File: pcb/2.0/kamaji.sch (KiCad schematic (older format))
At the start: 44 parts, among them J1 RJ10, J2 RJ10, J3 RJ10, J4 RJ10, J5 RJ10, J6 Daughter board, J7 ICSP, J8 USB_B, J9 USB_A, Q1 IRL540N, Q2 IRL540N, Q3 IRL540N, SW1 SW_Push, SW2 SW_Push, SW3 SW_Push, U1 ATMEGA32U4-AU, Y1 16MHz

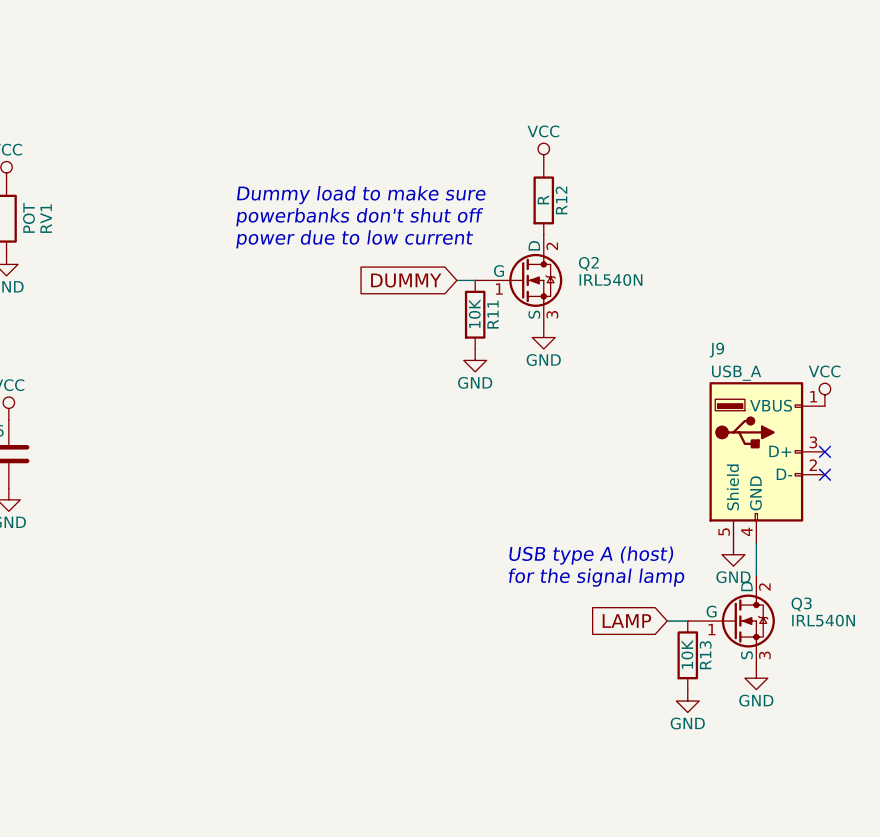
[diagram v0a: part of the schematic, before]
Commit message: use 4 parallel resistors for the dummy load
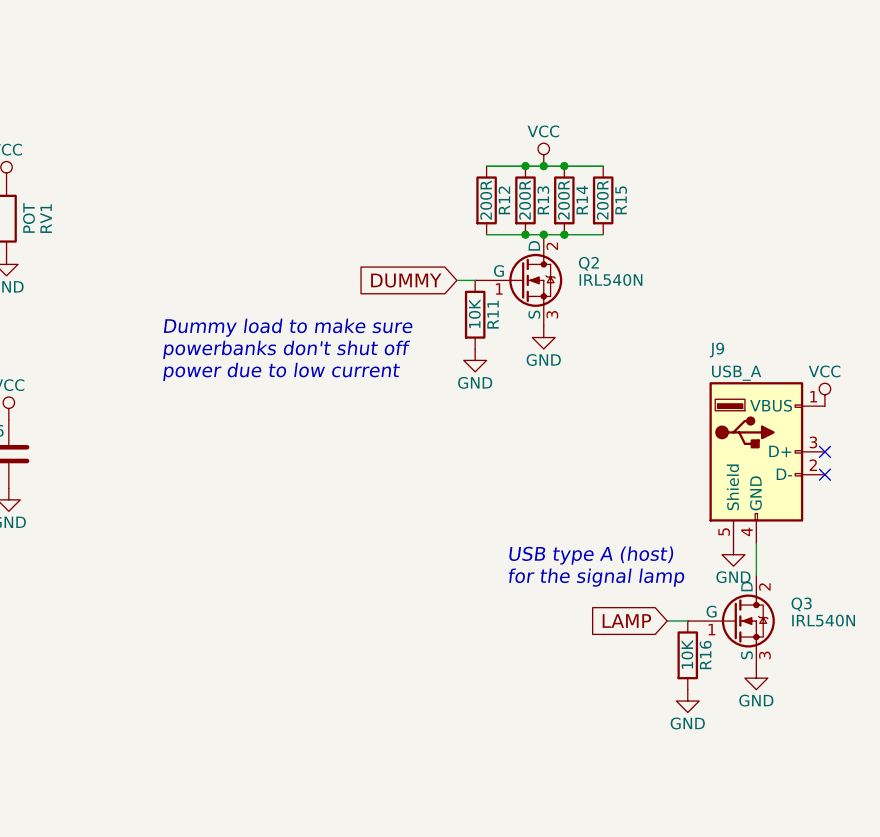
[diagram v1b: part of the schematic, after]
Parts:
- added R12, R13, R15: 200R, symbol R
- R14: renamed from R12; value R -> 200R
- renumbered R13 to R16
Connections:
- wire segments 82 -> 84
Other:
- moved on the sheet: R14

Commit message: start mapping symbols to footprints
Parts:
- F1: value 500mA -> 1A
- Q1, Q2, Q3: footprint TO_SOT_Packages_THT:TO-220_Vertical -> TO_SOT_Packages_THT:TO-220-3_Horizontal
- RV1: value POT -> 10K
- U1: footprint TQFP44 -> Housings_QFP:TQFP-44_10x10mm_Pitch0.8mm
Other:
- note added: "Control buttons use the internal pull-ups"

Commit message: use a graphic display instead of 2004
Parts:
- removed C6: 0.1uF, symbol C
- removed DS1: WC1602A, Displays:WC1602A, symbol WC1602A
- removed RV1: 10K, symbol POT
- added DS1: LCD12864B, kamaji:LCD12864B, symbol LCD12864B
- added R17, R18: 10K, symbol R
- R9: value 220R -> 10K
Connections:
- net labels added: LCD_CS, LCD_RST
- net labels removed: LCD_D4, LCD_D5, LCD_D6, LCD_D7, LCD_EN, LCD_RS
- wire segments 84 -> 80
- no-connect marks 3 -> 9
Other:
- note added: "Break for current\nmeasurement"
- note added: "Disconnect speaker\nwhen programmimg\nto avoid interference"
- note added: "ST7920-based LCD\ndisplay in serial mode"
- note removed: "Any HD44780 compatible LCD"
- moved on the sheet: F1, Q2, R11, R12, R13, R14, R15

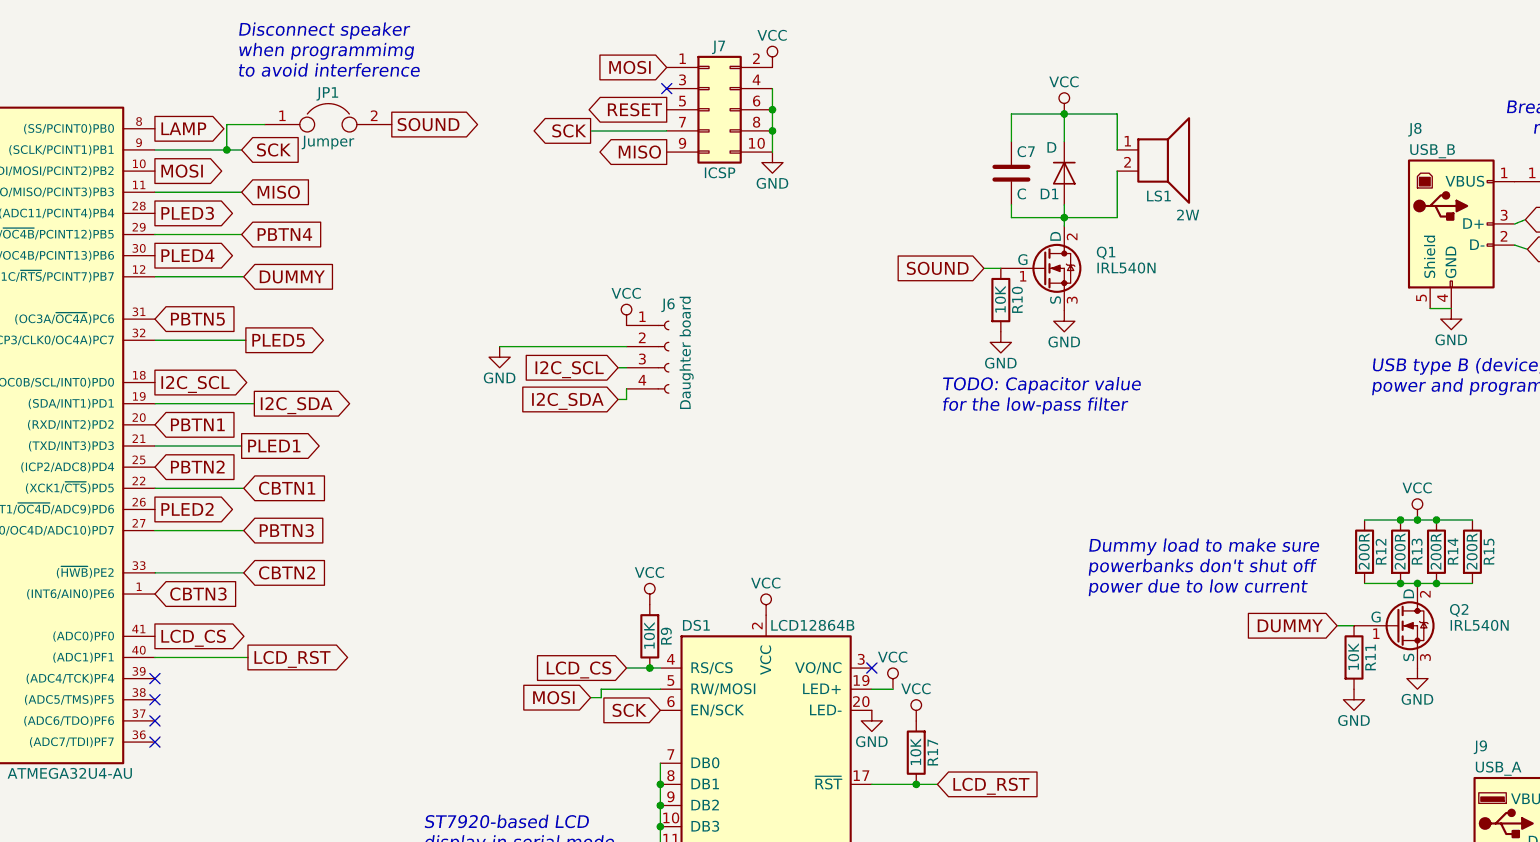
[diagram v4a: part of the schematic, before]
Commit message: pcb: delete the sound circuit
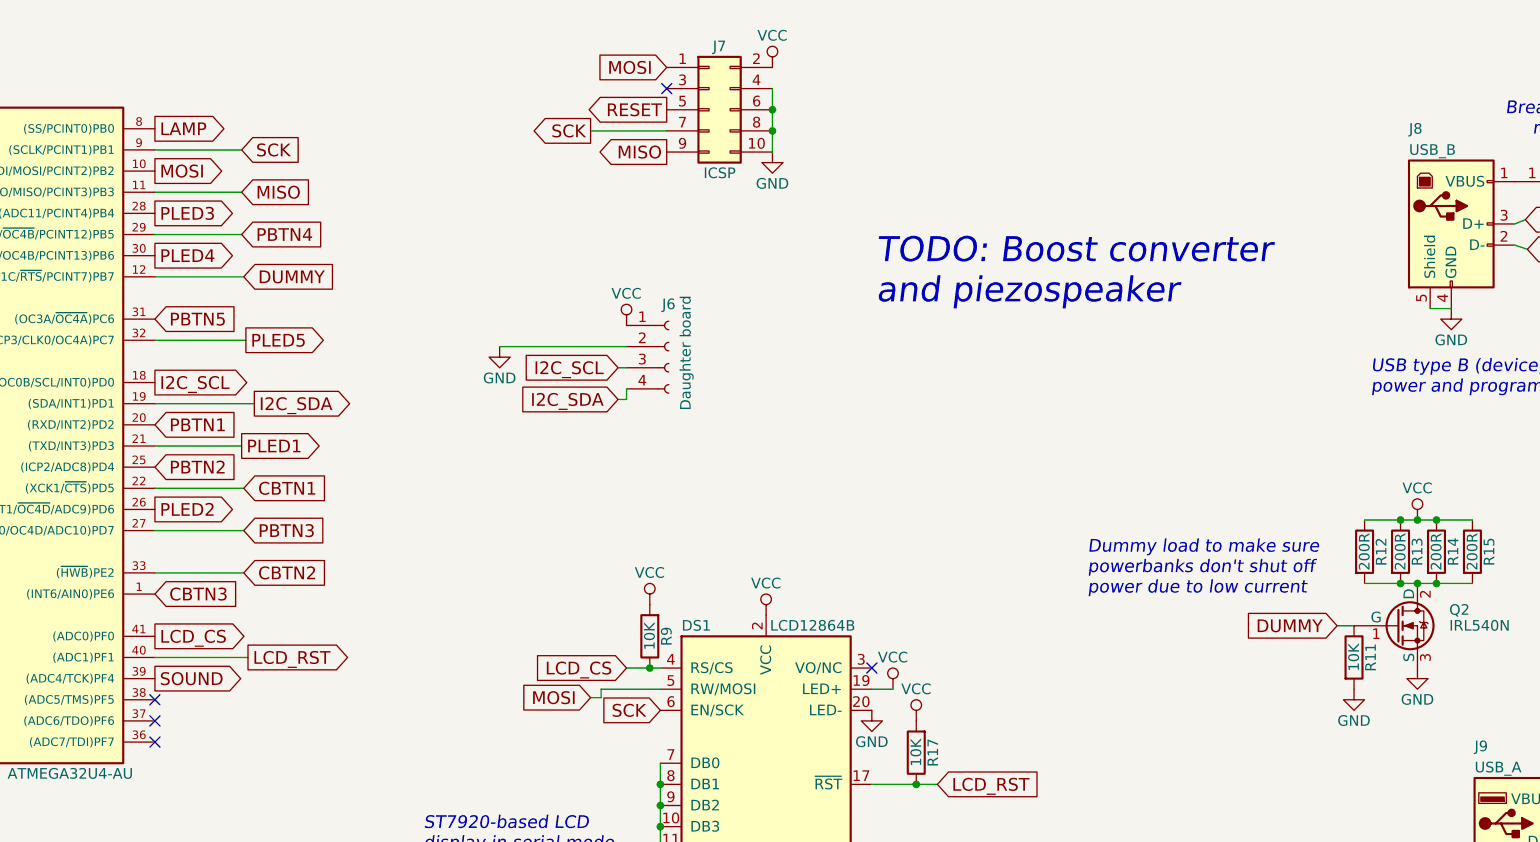
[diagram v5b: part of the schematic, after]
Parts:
- removed C7: C, symbol C
- removed D1: D, symbol D
- removed JP1: Jumper, symbol Jumper
- removed LS1: 2W, symbol Speaker
- removed Q1: IRL540N, TO_SOT_Packages_THT:TO-220-3_Horizontal, symbol IRLIZ44N
- removed R10: 10K, symbol R
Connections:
- net SOUND: now also U1.39 ((ADC4/TCK)PF4)
- no-connect marks 9 -> 8
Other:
- note added: "TODO: Boost converter\nand piezospeaker"
- note removed: "Disconnect speaker\nwhen programmimg\nto avoid interference"
- note removed: "TODO: Capacitor value\nfor the low-pass filter"
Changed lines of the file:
@@
 LIBS:kamaji
 LIBS:switches
+LIBS:kamaji-cache
 EELAYER 25 0
 EELAYER END
@@
 $EndComp
 $Comp
-L Speaker LS1
-U 1 1 59EB0736
-P 8480 1580
-F 0 "LS1" H 8540 1360 50  0000 R CNN
-F 1 "2W" H 8670 1270 50  0000 R CNN
-F 2 "" H 8480 1380 50  0001 C CNN
-F 3 "" H 8470 1530 50  0001 C CNN
-	1    8480 1580
-	1    0    0    -1
-$EndComp
-$Comp
-L D D1
-U 1 1 59EB079D
-P 8030 1690
-F 0 "D1" V 8130 1620 50  0000 C CNN
-F 1 "D" V 7910 1630 50  0000 C CNN
-F 2 "" H 8030 1690 50  0001 C CNN
-F 3 "" H 8030 1690 50  0001 C CNN
-	1    8030 1690
-	0    1    1    0
-$EndComp
-$Comp
-L VCC #PWR09
-U 1 1 59EB08CE
-P 8030 1410
-F 0 "#PWR09" H 8030 1260 50  0001 C CNN
-F 1 "VCC" H 8030 1560 50  0000 C CNN
-F 2 "" H 8030 1410 50  0001 C CNN
-F 3 "" H 8030 1410 50  0001 C CNN
-	1    8030 1410
-	1    0    0    -1
-$EndComp
-$Comp
-L C C7
-U 1 1 59EB0A92
-P 7780 1690
-F 0 "C7" H 7805 1790 50  0000 L CNN
-F 1 "C" H 7805 1590 50  0000 L CNN
-F 2 "" H 7818 1540 50  0001 C CNN
-F 3 "" H 7780 1690 50  0001 C CNN
-	1    7780 1690
-	1    0    0    -1
-$EndComp
-$Comp
-L IRLIZ44N Q1
-U 1 1 59EB0BD7
-P 7930 2140
-F 0 "Q1" H 8180 2215 50  0000 L CNN
-F 1 "IRL540N" H 8180 2140 50  0000 L CNN
-F 2 "TO_SOT_Packages_THT:TO-220-3_Horizontal" H 8180 2065 50  0001 L CIN
-F 3 "" H 7930 2140 50  0001 L CNN
-	1    7930 2140
-	1    0    0    -1
-$EndComp
-$Comp
-L GND #PWR010
-U 1 1 59EB0F4B
-P 8030 2340
-F 0 "#PWR010" H 8030 2090 50  0001 C CNN
-F 1 "GND" H 8030 2190 50  0000 C CNN
-F 2 "" H 8030 2340 50  0001 C CNN
-F 3 "" H 8030 2340 50  0001 C CNN
-	1    8030 2340
-	1    0    0    -1
-$EndComp
-$Comp
-L R R10
-U 1 1 59EB0FF4
-P 7730 2290
-F 0 "R10" V 7810 2290 50  0000 C CNN
-F 1 "10K" V 7730 2290 50  0000 C CNN
-F 2 "" V 7660 2290 50  0001 C CNN
-F 3 "" H 7730 2290 50  0001 C CNN
-	1    7730 2290
-	1    0    0    -1
-$EndComp
-$Comp
-L GND #PWR011
-U 1 1 59EB105E
-P 7730 2440
-F 0 "#PWR011" H 7730 2190 50  0001 C CNN
-F 1 "GND" H 7730 2290 50  0000 C CNN
-F 2 "" H 7730 2440 50  0001 C CNN
-F 3 "" H 7730 2440 50  0001 C CNN
-	1    7730 2440
-	1    0    0    -1
-$EndComp
-Text GLabel 7650 2140 0    60   Input ~ 0
-SOUND
-$Comp
 L Conn_02x05_Odd_Even J7
 U 1 1 59EB13A5
@@
 Text GLabel 6150 1190 0    60   Input ~ 0
 MOSI
-Text Notes 7450 2830 0    60   Italic 0
-TODO: Capacitor value\nfor the low-pass filter
 NoConn ~ 6150 1290
 $Comp
@@
 Text GLabel 4140 1580 2    60   Input ~ 0
 SCK
-$Comp
-L Jumper JP1
-U 1 1 59EB71E9
-P 4550 1460
-F 0 "JP1" H 4550 1610 50  0000 C CNN
-F 1 "Jumper" H 4550 1380 50  0000 C CNN
-F 2 "" H 4550 1460 50  0001 C CNN
-F 3 "" H 4550 1460 50  0001 C CNN
-	1    4550 1460
-	1    0    0    -1
-$EndComp
-Text GLabel 4850 1460 2    60   Output ~ 0
+Text GLabel 3730 4080 2    60   Output ~ 0
 SOUND
 $Comp
@@
 	9320 3830 9400 3830
 Wire Wire Line
-	7780 1410 8280 1410
-Wire Wire Line
-	8280 1410 8280 1580
-Wire Wire Line
-	7780 1540 7780 1410
-Wire Wire Line
-	8030 1840 8030 1940
-Wire Wire Line
-	8030 1540 8030 1410
-Connection ~ 8030 1410
-Wire Wire Line
-	7650 2140 7730 2140
-Wire Wire Line
 	6650 1290 6650 1590
 Connection ~ 6650 1390
@@
 	10210 1910 10160 1930
 Wire Wire Line
-	7780 1840 7780 1900
-Wire Wire Line
-	7780 1900 8280 1900
-Connection ~ 8030 1900
-Wire Wire Line
-	8280 1900 8280 1680
-Wire Wire Line
 	1600 7050 1750 7050
 Wire Wire Line
@@
 Wire Wire Line
 	3730 1580 4140 1580
-Wire Wire Line
-	4250 1460 4070 1460
-Wire Wire Line
-	4070 1460 4070 1580
-Connection ~ 4070 1580
 Wire Wire Line
 	9450 3630 9960 3630
@@
 Wire Wire Line
 	4170 3980 3730 3980
-NoConn ~ 3730 4080
 NoConn ~ 3730 4180
 NoConn ~ 3730 4280
@@
 	1    0    0    -1
 $EndComp
-Text Notes 4120 1250 0    60   Italic 0
-Disconnect speaker\nwhen programmimg\nto avoid interference
 Wire Wire Line
 	10940 1730 10760 1730
 Text Notes 10820 1520 2    60   Italic 0
 Break for current\nmeasurement
+Text Notes 7140 2320 0    118  Italic 0
+TODO: Boost converter\nand piezospeaker
 $EndSCHEMATC

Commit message: minor pcb changes
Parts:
- added C?: 0.1uF, symbol C
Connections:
- net GND: now also C?.2
- net VCC: now also C?.1
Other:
- moved on the sheet: C3, C4
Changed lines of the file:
@@
 L C C3
 U 1 1 59EB7B64
-P 1030 4610
-F 0 "C3" H 920 4710 50  0000 L CNN
-F 1 "0.1uF" H 790 4520 50  0000 L CNN
-F 2 "" H 1068 4460 50  0001 C CNN
-F 3 "" H 1030 4610 50  0001 C CNN
-	1    1030 4610
+P 910 5010
+F 0 "C3" H 800 5110 50  0000 L CNN
+F 1 "0.1uF" H 670 4920 50  0000 L CNN
+F 2 "" H 948 4860 50  0001 C CNN
+F 3 "" H 910 5010 50  0001 C CNN
+	1    910  5010
 	1    0    0    -1
 $EndComp
@@
 L GND #PWR034
 U 1 1 59EB7C3A
-P 1030 4760
-F 0 "#PWR034" H 1030 4510 50  0001 C CNN
-F 1 "GND" H 1030 4610 50  0000 C CNN
-F 2 "" H 1030 4760 50  0001 C CNN
-F 3 "" H 1030 4760 50  0001 C CNN
-	1    1030 4760
+P 910 5160
+F 0 "#PWR034" H 910 4910 50  0001 C CNN
+F 1 "GND" H 910 5010 50  0000 C CNN
+F 2 "" H 910 5160 50  0001 C CNN
+F 3 "" H 910 5160 50  0001 C CNN
+	1    910  5160
 	1    0    0    -1
 $EndComp
@@
 L VCC #PWR035
 U 1 1 59EB7CBD
-P 1030 4460
-F 0 "#PWR035" H 1030 4310 50  0001 C CNN
-F 1 "VCC" H 1030 4610 50  0000 C CNN
-F 2 "" H 1030 4460 50  0001 C CNN
-F 3 "" H 1030 4460 50  0001 C CNN
-	1    1030 4460
+P 910 4860
+F 0 "#PWR035" H 910 4710 50  0001 C CNN
+F 1 "VCC" H 910 5010 50  0000 C CNN
+F 2 "" H 910 4860 50  0001 C CNN
+F 3 "" H 910 4860 50  0001 C CNN
+	1    910  4860
 	1    0    0    -1
 $EndComp
@@
 L C C4
 U 1 1 59EB7D86
-P 1390 4610
-F 0 "C4" H 1280 4710 50  0000 L CNN
-F 1 "0.1uF" H 1150 4520 50  0000 L CNN
-F 2 "" H 1428 4460 50  0001 C CNN
-F 3 "" H 1390 4610 50  0001 C CNN
-	1    1390 4610
+P 1270 5010
+F 0 "C4" H 1160 5110 50  0000 L CNN
+F 1 "0.1uF" H 1030 4920 50  0000 L CNN
+F 2 "" H 1308 4860 50  0001 C CNN
+F 3 "" H 1270 5010 50  0001 C CNN
+	1    1270 5010
 	1    0    0    -1
 $EndComp
@@
 L GND #PWR036
 U 1 1 59EB7D8C
-P 1390 4760
-F 0 "#PWR036" H 1390 4510 50  0001 C CNN
-F 1 "GND" H 1390 4610 50  0000 C CNN
-F 2 "" H 1390 4760 50  0001 C CNN
-F 3 "" H 1390 4760 50  0001 C CNN
-	1    1390 4760
+P 1270 5160
+F 0 "#PWR036" H 1270 4910 50  0001 C CNN
+F 1 "GND" H 1270 5010 50  0000 C CNN
+F 2 "" H 1270 5160 50  0001 C CNN
+F 3 "" H 1270 5160 50  0001 C CNN
+	1    1270 5160
 	1    0    0    -1
 $EndComp
@@
 L VCC #PWR037
 U 1 1 59EB7D92
-P 1390 4460
-F 0 "#PWR037" H 1390 4310 50  0001 C CNN
-F 1 "VCC" H 1390 4610 50  0000 C CNN
-F 2 "" H 1390 4460 50  0001 C CNN
-F 3 "" H 1390 4460 50  0001 C CNN
-	1    1390 4460
+P 1270 4860
+F 0 "#PWR037" H 1270 4710 50  0001 C CNN
+F 1 "VCC" H 1270 5010 50  0000 C CNN
+F 2 "" H 1270 4860 50  0001 C CNN
+F 3 "" H 1270 4860 50  0001 C CNN
+	1    1270 4860
 	1    0    0    -1
 $EndComp
@@
 Text Notes 7140 2320 0    118  Italic 0
 TODO: Boost converter\nand piezospeaker
+$Comp
+L C C?
+U 1 1 5A15E885
+P 1620 5010
+F 0 "C?" H 1510 5110 50  0000 L CNN
+F 1 "0.1uF" H 1380 4920 50  0000 L CNN
+F 2 "" H 1658 4860 50  0001 C CNN
+F 3 "" H 1620 5010 50  0001 C CNN
+	1    1620 5010
+	1    0    0    -1
+$EndComp
+$Comp
+L GND #PWR?
+U 1 1 5A15E88B
+P 1620 5160
+F 0 "#PWR?" H 1620 4910 50  0001 C CNN
+F 1 "GND" H 1620 5010 50  0000 C CNN
+F 2 "" H 1620 5160 50  0001 C CNN
+F 3 "" H 1620 5160 50  0001 C CNN
+	1    1620 5160
+	1    0    0    -1
+$EndComp
+$Comp
+L VCC #PWR?
+U 1 1 5A15E891
+P 1620 4860
+F 0 "#PWR?" H 1620 4710 50  0001 C CNN
+F 1 "VCC" H 1620 5010 50  0000 C CNN
+F 2 "" H 1620 4860 50  0001 C CNN
+F 3 "" H 1620 4860 50  0001 C CNN
+	1    1620 4860
+	1    0    0    -1
+$EndComp
 $EndSCHEMATC
